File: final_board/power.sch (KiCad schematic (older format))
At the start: 3 parts, among them U501 MCP1755-33, U502 MCP1755-5

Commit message: Changed CAN Chip, added capacitors, added reference
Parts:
- added C501, C503: 10μ, Capacitors_SMD:C_0805_HandSoldering, symbol C
- added C502, C504: .1μ, Capacitors_SMD:C_0603_HandSoldering, symbol C
- gave numbers to parts that had none: 1
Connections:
- wire segments 12 -> 20
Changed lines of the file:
@@
 EESchema Schematic File Version 2
-LIBS:final_outline-rescue
 LIBS:power
 LIBS:device
@@
 $EndComp
 $Comp
-L GND #PWR019
+L GND #PWR017
 U 1 1 563E6C39
 P 5350 3700
-F 0 "#PWR019" H 5350 3450 50  0001 C CNN
+F 0 "#PWR017" H 5350 3450 50  0001 C CNN
 F 1 "GND" H 5350 3550 50  0000 C CNN
 F 2 "" H 5350 3700 60  0000 C CNN
@@
 $EndComp
 $Comp
-L GND #PWR020
+L GND #PWR018
 U 1 1 5650E5B7
 P 2350 3700
-F 0 "#PWR020" H 2350 3450 50  0001 C CNN
+F 0 "#PWR018" H 2350 3450 50  0001 C CNN
 F 1 "GND" H 2350 3550 50  0000 C CNN
 F 2 "" H 2350 3700 60  0000 C CNN
@@
 +12V
 Wire Wire Line
-	1300 2900 1850 2900
+	1000 2900 1850 2900
 Wire Wire Line
 	1600 2900 1600 3100
@@
 Connection ~ 3550 2900
 $Comp
-L LM7810CT U?
+L LM7810CT U503
 U 1 1 56914C23
 P 2300 1600
-F 0 "U?" H 2100 1800 50  0000 C CNN
+F 0 "U503" H 2100 1800 50  0000 C CNN
 F 1 "LM7810CT" H 2300 1800 50  0000 L CNN
 F 2 "TO-220" H 2300 1700 50  0000 C CIN
@@
 +10V
 $Comp
-L GND #PWR021
+L GND #PWR019
 U 1 1 56914D13
 P 2300 1950
-F 0 "#PWR021" H 2300 1700 50  0001 C CNN
+F 0 "#PWR019" H 2300 1700 50  0001 C CNN
 F 1 "GND" H 2300 1800 50  0000 C CNN
 F 2 "" H 2300 1950 50  0000 C CNN
@@
 Wire Wire Line
 	2300 1950 2300 1850
-Text HLabel 1300 2900 0    60   Input ~ 0
+Text HLabel 1000 2900 0    60   Input ~ 0
 +12V
+$Comp
+L C C503
+U 1 1 569165B3
+P 4100 3200
+F 0 "C503" H 4125 3300 50  0000 L CNN
+F 1 "10μ" H 4125 3100 50  0000 L CNN
+F 2 "Capacitors_SMD:C_0805_HandSoldering" H 4138 3050 50  0001 C CNN
+F 3 "" H 4100 3200 50  0000 C CNN
+	1    4100 3200
+	1    0    0    -1
+$EndComp
+$Comp
+L C C504
+U 1 1 5691663C
+P 4400 3200
+F 0 "C504" H 4425 3300 50  0000 L CNN
+F 1 ".1μ" H 4425 3100 50  0000 L CNN
+F 2 "Capacitors_SMD:C_0603_HandSoldering" H 4438 3050 50  0001 C CNN
+F 3 "" H 4400 3200 50  0000 C CNN
+	1    4400 3200
+	1    0    0    -1
+$EndComp
+$Comp
+L C C502
+U 1 1 56916685
+P 1450 3200
+F 0 "C502" H 1475 3300 50  0000 L CNN
+F 1 ".1μ" H 1475 3100 50  0000 L CNN
+F 2 "Capacitors_SMD:C_0603_HandSoldering" H 1488 3050 50  0001 C CNN
+F 3 "" H 1450 3200 50  0000 C CNN
+	1    1450 3200
+	1    0    0    -1
+$EndComp
+$Comp
+L C C501
+U 1 1 569166FC
+P 1200 3200
+F 0 "C501" H 1225 3300 50  0000 L CNN
+F 1 "10μ" H 1225 3100 50  0000 L CNN
+F 2 "Capacitors_SMD:C_0805_HandSoldering" H 1238 3050 50  0001 C CNN
+F 3 "" H 1200 3200 50  0000 C CNN
+	1    1200 3200
+	1    0    0    -1
+$EndComp
+Wire Wire Line
+	1200 3050 1200 2900
+Connection ~ 1200 2900
+Wire Wire Line
+	1450 3050 1450 2900
+Connection ~ 1450 2900
+Wire Wire Line
+	4400 2900 4400 3050
+Connection ~ 4400 2900
+Wire Wire Line
+	4100 2900 4100 3050
+Connection ~ 4100 2900
+$Comp
+L GND #PWR020
+U 1 1 5691687F
+P 4400 3650
+F 0 "#PWR020" H 4400 3400 50  0001 C CNN
+F 1 "GND" H 4400 3500 50  0000 C CNN
+F 2 "" H 4400 3650 50  0000 C CNN
+F 3 "" H 4400 3650 50  0000 C CNN
+	1    4400 3650
+	1    0    0    -1
+$EndComp
+$Comp
+L GND #PWR021
+U 1 1 569168A1
+P 4100 3650
+F 0 "#PWR021" H 4100 3400 50  0001 C CNN
+F 1 "GND" H 4100 3500 50  0000 C CNN
+F 2 "" H 4100 3650 50  0000 C CNN
+F 3 "" H 4100 3650 50  0000 C CNN
+	1    4100 3650
+	1    0    0    -1
+$EndComp
+$Comp
+L GND #PWR022
+U 1 1 569168C3
+P 1450 3600
+F 0 "#PWR022" H 1450 3350 50  0001 C CNN
+F 1 "GND" H 1450 3450 50  0000 C CNN
+F 2 "" H 1450 3600 50  0000 C CNN
+F 3 "" H 1450 3600 50  0000 C CNN
+	1    1450 3600
+	1    0    0    -1
+$EndComp
+$Comp
+L GND #PWR023
+U 1 1 569168E5
+P 1200 3600
+F 0 "#PWR023" H 1200 3350 50  0001 C CNN
+F 1 "GND" H 1200 3450 50  0000 C CNN
+F 2 "" H 1200 3600 50  0000 C CNN
+F 3 "" H 1200 3600 50  0000 C CNN
+	1    1200 3600
+	1    0    0    -1
+$EndComp
+Wire Wire Line
+	4100 3350 4100 3650
+Wire Wire Line
+	4400 3350 4400 3650
+Wire Wire Line
+	1200 3350 1200 3600
+Wire Wire Line
+	1450 3350 1450 3600
 $EndSCHEMATC

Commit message: Final changes to board
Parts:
- removed U503: LM7810CT, TO-220, symbol LM7810CT
- added C505: 10μ, Capacitors_SMD:C_0805_HandSoldering, symbol C
- added C506: .1μ, Capacitors_SMD:C_0603_HandSoldering, symbol C
- added U503: Zsr1000gta, TO_SOT_Packages_SMD:SOT-223, symbol Zsr1000gta
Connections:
- wire segments 20 -> 27
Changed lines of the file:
@@
 LIBS:MITEVT_power
 LIBS:MITEVT_REG
+LIBS:zsr1000gta
 LIBS:final_outline-cache
 EELAYER 25 0
@@
 $EndComp
 $Comp
-L GND #PWR017
+L GND #PWR018
 U 1 1 563E6C39
 P 5350 3700
-F 0 "#PWR017" H 5350 3450 50  0001 C CNN
+F 0 "#PWR018" H 5350 3450 50  0001 C CNN
 F 1 "GND" H 5350 3550 50  0000 C CNN
 F 2 "" H 5350 3700 60  0000 C CNN
@@
 $EndComp
 $Comp
-L GND #PWR018
+L GND #PWR019
 U 1 1 5650E5B7
 P 2350 3700
-F 0 "#PWR018" H 2350 3450 50  0001 C CNN
+F 0 "#PWR019" H 2350 3450 50  0001 C CNN
 F 1 "GND" H 2350 3550 50  0000 C CNN
 F 2 "" H 2350 3700 60  0000 C CNN
@@
 	2350 3500 2350 3700
 NoConn ~ 2900 3100
-Text HLabel 1900 1550 0    60   Input ~ 0
+Text HLabel 1550 1550 0    60   Input ~ 0
 +12V
 Wire Wire Line
@@
 	3550 2600 3550 2900
 Connection ~ 3550 2900
-$Comp
-L LM7810CT U503
-U 1 1 56914C23
-P 2300 1600
-F 0 "U503" H 2100 1800 50  0000 C CNN
-F 1 "LM7810CT" H 2300 1800 50  0000 L CNN
-F 2 "TO-220" H 2300 1700 50  0000 C CIN
-F 3 "" H 2300 1600 50  0000 C CNN
-	1    2300 1600
-	1    0    0    -1
-$EndComp
-Text HLabel 2700 1550 2    60   Output ~ 0
+Text HLabel 3100 1550 2    60   Output ~ 0
 +10V
 $Comp
-L GND #PWR019
+L GND #PWR020
 U 1 1 56914D13
-P 2300 1950
-F 0 "#PWR019" H 2300 1700 50  0001 C CNN
-F 1 "GND" H 2300 1800 50  0000 C CNN
-F 2 "" H 2300 1950 50  0000 C CNN
-F 3 "" H 2300 1950 50  0000 C CNN
-	1    2300 1950
-	1    0    0    -1
-$EndComp
-Wire Wire Line
-	2300 1950 2300 1850
+P 2250 1950
+F 0 "#PWR020" H 2250 1700 50  0001 C CNN
+F 1 "GND" H 2250 1800 50  0000 C CNN
+F 2 "" H 2250 1950 50  0000 C CNN
+F 3 "" H 2250 1950 50  0000 C CNN
+	1    2250 1950
+	1    0    0    -1
+$EndComp
 Text HLabel 1000 2900 0    60   Input ~ 0
 +12V
@@
 Connection ~ 4100 2900
 $Comp
-L GND #PWR020
+L GND #PWR021
 U 1 1 5691687F
 P 4400 3650
-F 0 "#PWR020" H 4400 3400 50  0001 C CNN
+F 0 "#PWR021" H 4400 3400 50  0001 C CNN
 F 1 "GND" H 4400 3500 50  0000 C CNN
 F 2 "" H 4400 3650 50  0000 C CNN
@@
 $EndComp
 $Comp
-L GND #PWR021
+L GND #PWR022
 U 1 1 569168A1
 P 4100 3650
-F 0 "#PWR021" H 4100 3400 50  0001 C CNN
+F 0 "#PWR022" H 4100 3400 50  0001 C CNN
 F 1 "GND" H 4100 3500 50  0000 C CNN
 F 2 "" H 4100 3650 50  0000 C CNN
@@
 $EndComp
 $Comp
-L GND #PWR022
+L GND #PWR023
 U 1 1 569168C3
 P 1450 3600
-F 0 "#PWR022" H 1450 3350 50  0001 C CNN
+F 0 "#PWR023" H 1450 3350 50  0001 C CNN
 F 1 "GND" H 1450 3450 50  0000 C CNN
 F 2 "" H 1450 3600 50  0000 C CNN
@@
 $EndComp
 $Comp
-L GND #PWR023
+L GND #PWR024
 U 1 1 569168E5
 P 1200 3600
-F 0 "#PWR023" H 1200 3350 50  0001 C CNN
+F 0 "#PWR024" H 1200 3350 50  0001 C CNN
 F 1 "GND" H 1200 3450 50  0000 C CNN
 F 2 "" H 1200 3600 50  0000 C CNN
@@
 Wire Wire Line
 	1450 3350 1450 3600
+Wire Wire Line
+	1900 1550 1550 1550
+Wire Wire Line
+	2700 1550 3100 1550
+$Comp
+L GND #PWR025
+U 1 1 56922780
+P 2400 1950
+F 0 "#PWR025" H 2400 1700 50  0001 C CNN
+F 1 "GND" H 2400 1800 50  0000 C CNN
+F 2 "" H 2400 1950 50  0000 C CNN
+F 3 "" H 2400 1950 50  0000 C CNN
+	1    2400 1950
+	1    0    0    -1
+$EndComp
+Wire Wire Line
+	2250 1850 2250 1950
+Wire Wire Line
+	2400 1850 2400 1950
+$Comp
+L Zsr1000gta U503
+U 1 1 56922D9F
+P 2300 1600
+F 0 "U503" H 2500 1400 50  0000 C CNN
+F 1 "Zsr1000gta" H 2300 1800 50  0000 C CNN
+F 2 "TO_SOT_Packages_SMD:SOT-223" H 2300 1600 50  0001 C CNN
+F 3 "" H 2300 1600 50  0000 C CNN
+	1    2300 1600
+	1    0    0    -1
+$EndComp
+$Comp
+L C C506
+U 1 1 56923C74
+P 3000 1850
+F 0 "C506" H 3025 1950 50  0000 L CNN
+F 1 ".1μ" H 3025 1750 50  0000 L CNN
+F 2 "Capacitors_SMD:C_0603_HandSoldering" H 3038 1700 50  0001 C CNN
+F 3 "" H 3000 1850 50  0000 C CNN
+	1    3000 1850
+	1    0    0    -1
+$EndComp
+$Comp
+L C C505
+U 1 1 56923C7A
+P 2750 1850
+F 0 "C505" H 2775 1950 50  0000 L CNN
+F 1 "10μ" H 2775 1750 50  0000 L CNN
+F 2 "Capacitors_SMD:C_0805_HandSoldering" H 2788 1700 50  0001 C CNN
+F 3 "" H 2750 1850 50  0000 C CNN
+	1    2750 1850
+	1    0    0    -1
+$EndComp
+$Comp
+L GND #PWR?
+U 1 1 56923C80
+P 3000 2250
+F 0 "#PWR?" H 3000 2000 50  0001 C CNN
+F 1 "GND" H 3000 2100 50  0000 C CNN
+F 2 "" H 3000 2250 50  0000 C CNN
+F 3 "" H 3000 2250 50  0000 C CNN
+	1    3000 2250
+	1    0    0    -1
+$EndComp
+$Comp
+L GND #PWR?
+U 1 1 56923C86
+P 2750 2250
+F 0 "#PWR?" H 2750 2000 50  0001 C CNN
+F 1 "GND" H 2750 2100 50  0000 C CNN
+F 2 "" H 2750 2250 50  0000 C CNN
+F 3 "" H 2750 2250 50  0000 C CNN
+	1    2750 2250
+	1    0    0    -1
+$EndComp
+Wire Wire Line
+	2750 2000 2750 2250
+Wire Wire Line
+	3000 2000 3000 2250
+Wire Wire Line
+	2750 1700 2750 1550
+Connection ~ 2750 1550
+Wire Wire Line
+	3000 1700 3000 1550
+Connection ~ 3000 1550
 $EndSCHEMATC

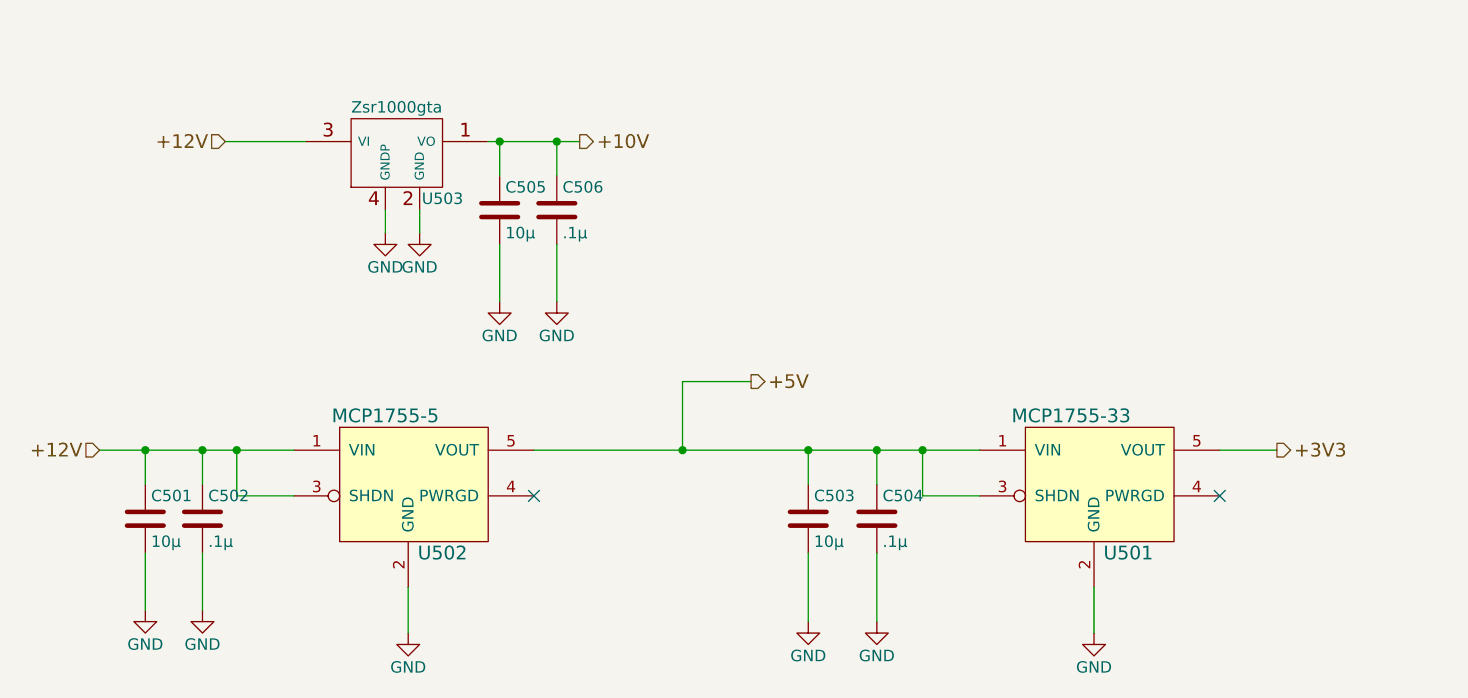
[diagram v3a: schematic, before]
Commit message: Updated PCB by replacing old parts, fixing voltage regulator, adding test points, and general improvements
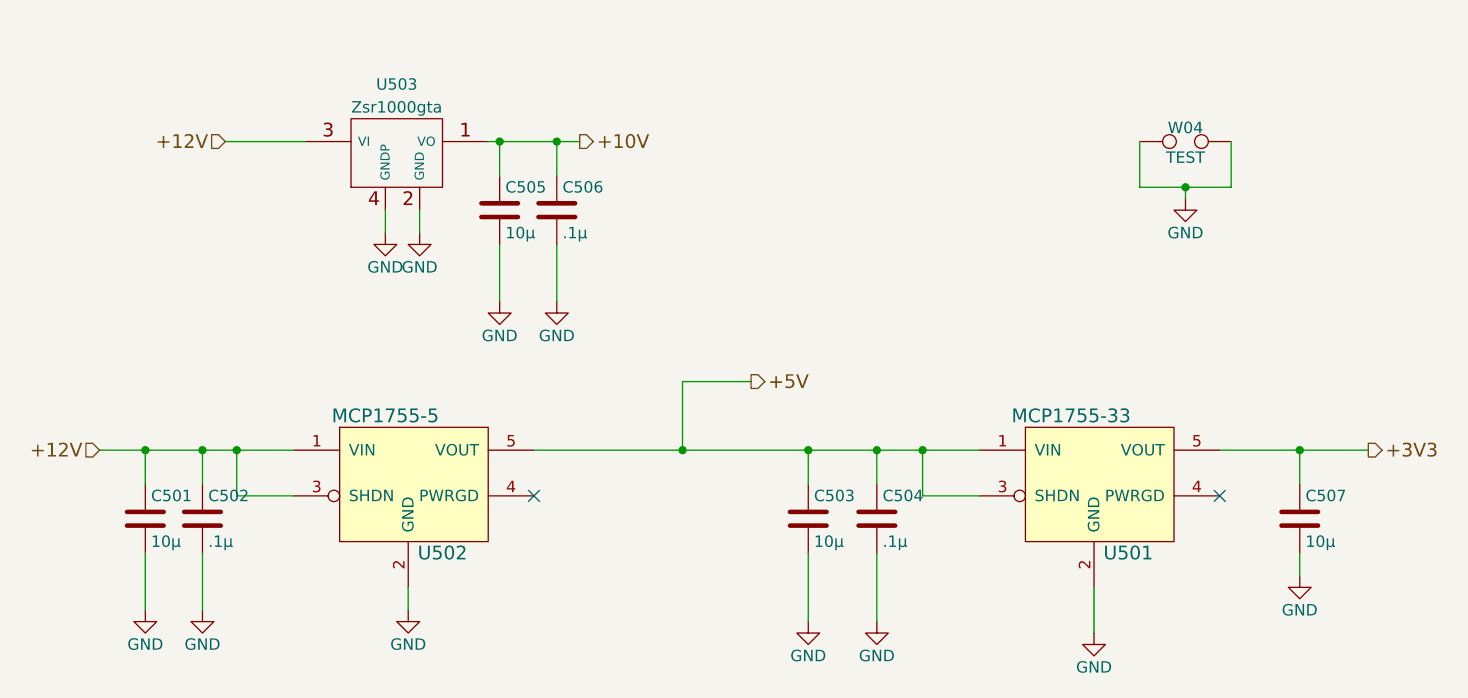
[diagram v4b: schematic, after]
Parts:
- added C507: 10μ, Capacitors_SMD:C_0805_HandSoldering, symbol C
- added W04: TEST, Measurement_Points:Test_Point_2Pads, symbol TEST
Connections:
- net +3V3: now also C507.1
- net GND: now also C507.2, W04.1, W04.2
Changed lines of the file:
@@
 $EndComp
 $Comp
-L GND #PWR018
+L GND #PWR026
 U 1 1 563E6C39
 P 5350 3700
-F 0 "#PWR018" H 5350 3450 50  0001 C CNN
+F 0 "#PWR026" H 5350 3450 50  0001 C CNN
 F 1 "GND" H 5350 3550 50  0000 C CNN
 F 2 "" H 5350 3700 60  0000 C CNN
@@
 	4600 3100 4850 3100
 Connection ~ 4600 2900
-Text HLabel 6150 2900 2    60   Output ~ 0
+Text HLabel 6550 2900 2    60   Output ~ 0
 +3V3
 Wire Wire Line
-	6150 2900 5900 2900
+	5900 2900 6550 2900
 $Comp
 L MCP1755 U502
@@
 $EndComp
 $Comp
-L GND #PWR019
+L GND #PWR027
 U 1 1 5650E5B7
-P 2350 3700
-F 0 "#PWR019" H 2350 3450 50  0001 C CNN
-F 1 "GND" H 2350 3550 50  0000 C CNN
-F 2 "" H 2350 3700 60  0000 C CNN
-F 3 "" H 2350 3700 60  0000 C CNN
-	1    2350 3700
-	1    0    0    -1
-$EndComp
-Wire Wire Line
-	2350 3500 2350 3700
+P 2350 3600
+F 0 "#PWR027" H 2350 3350 50  0001 C CNN
+F 1 "GND" H 2350 3450 50  0000 C CNN
+F 2 "" H 2350 3600 60  0000 C CNN
+F 3 "" H 2350 3600 60  0000 C CNN
+	1    2350 3600
+	1    0    0    -1
+$EndComp
 NoConn ~ 2900 3100
 Text HLabel 1550 1550 0    60   Input ~ 0
@@
 +10V
 $Comp
-L GND #PWR020
+L GND #PWR028
 U 1 1 56914D13
 P 2250 1950
-F 0 "#PWR020" H 2250 1700 50  0001 C CNN
+F 0 "#PWR028" H 2250 1700 50  0001 C CNN
 F 1 "GND" H 2250 1800 50  0000 C CNN
 F 2 "" H 2250 1950 50  0000 C CNN
@@
 Connection ~ 4100 2900
 $Comp
-L GND #PWR021
+L GND #PWR029
 U 1 1 5691687F
 P 4400 3650
-F 0 "#PWR021" H 4400 3400 50  0001 C CNN
+F 0 "#PWR029" H 4400 3400 50  0001 C CNN
 F 1 "GND" H 4400 3500 50  0000 C CNN
 F 2 "" H 4400 3650 50  0000 C CNN
@@
 $EndComp
 $Comp
-L GND #PWR022
+L GND #PWR030
 U 1 1 569168A1
 P 4100 3650
-F 0 "#PWR022" H 4100 3400 50  0001 C CNN
+F 0 "#PWR030" H 4100 3400 50  0001 C CNN
 F 1 "GND" H 4100 3500 50  0000 C CNN
 F 2 "" H 4100 3650 50  0000 C CNN
@@
 $EndComp
 $Comp
-L GND #PWR023
+L GND #PWR031
 U 1 1 569168C3
 P 1450 3600
-F 0 "#PWR023" H 1450 3350 50  0001 C CNN
+F 0 "#PWR031" H 1450 3350 50  0001 C CNN
 F 1 "GND" H 1450 3450 50  0000 C CNN
 F 2 "" H 1450 3600 50  0000 C CNN
@@
 $EndComp
 $Comp
-L GND #PWR024
+L GND #PWR032
 U 1 1 569168E5
 P 1200 3600
-F 0 "#PWR024" H 1200 3350 50  0001 C CNN
+F 0 "#PWR032" H 1200 3350 50  0001 C CNN
 F 1 "GND" H 1200 3450 50  0000 C CNN
 F 2 "" H 1200 3600 50  0000 C CNN
@@
 	2700 1550 3100 1550
 $Comp
-L GND #PWR025
+L GND #PWR033
 U 1 1 56922780
 P 2400 1950
-F 0 "#PWR025" H 2400 1700 50  0001 C CNN
+F 0 "#PWR033" H 2400 1700 50  0001 C CNN
 F 1 "GND" H 2400 1800 50  0000 C CNN
 F 2 "" H 2400 1950 50  0000 C CNN
@@
 U 1 1 56922D9F
 P 2300 1600
-F 0 "U503" H 2500 1400 50  0000 C CNN
+F 0 "U503" H 2300 1900 50  0000 C CNN
 F 1 "Zsr1000gta" H 2300 1800 50  0000 C CNN
 F 2 "TO_SOT_Packages_SMD:SOT-223" H 2300 1600 50  0001 C CNN
@@
 $EndComp
 $Comp
-L GND #PWR026
+L GND #PWR034
 U 1 1 56923C80
 P 3000 2250
-F 0 "#PWR026" H 3000 2000 50  0001 C CNN
+F 0 "#PWR034" H 3000 2000 50  0001 C CNN
 F 1 "GND" H 3000 2100 50  0000 C CNN
 F 2 "" H 3000 2250 50  0000 C CNN
@@
 $EndComp
 $Comp
-L GND #PWR027
+L GND #PWR035
 U 1 1 56923C86
 P 2750 2250
-F 0 "#PWR027" H 2750 2000 50  0001 C CNN
+F 0 "#PWR035" H 2750 2000 50  0001 C CNN
 F 1 "GND" H 2750 2100 50  0000 C CNN
 F 2 "" H 2750 2250 50  0000 C CNN
@@
 	3000 1700 3000 1550
 Connection ~ 3000 1550
+$Comp
+L C C507
+U 1 1 5825A458
+P 6250 3200
+F 0 "C507" H 6275 3300 50  0000 L CNN
+F 1 "10μ" H 6275 3100 50  0000 L CNN
+F 2 "Capacitors_SMD:C_0805_HandSoldering" H 6288 3050 50  0001 C CNN
+F 3 "" H 6250 3200 50  0000 C CNN
+	1    6250 3200
+	1    0    0    -1
+$EndComp
+Wire Wire Line
+	6250 3050 6250 2900
+Connection ~ 6250 2900
+Wire Wire Line
+	6250 3350 6250 3450
+$Comp
+L GND #PWR036
+U 1 1 5825A5A4
+P 6250 3450
+F 0 "#PWR036" H 6250 3200 50  0001 C CNN
+F 1 "GND" H 6250 3300 50  0000 C CNN
+F 2 "" H 6250 3450 50  0000 C CNN
+F 3 "" H 6250 3450 50  0000 C CNN
+	1    6250 3450
+	1    0    0    -1
+$EndComp
+Wire Wire Line
+	2350 3500 2350 3600
+$Comp
+L TEST W04
+U 1 1 5827D5C6
+P 5750 1550
+F 0 "W04" H 5750 1610 50  0000 C CNN
+F 1 "TEST" H 5750 1480 50  0000 C CNN
+F 2 "Measurement_Points:Test_Point_2Pads" H 5750 1550 50  0001 C CNN
+F 3 "" H 5750 1550 50  0000 C CNN
+	1    5750 1550
+	1    0    0    -1
+$EndComp
+Wire Wire Line
+	5550 1550 5550 1750
+Wire Wire Line
+	5550 1750 5950 1750
+Wire Wire Line
+	5950 1750 5950 1550
+Wire Wire Line
+	5750 1750 5750 1800
+Connection ~ 5750 1750
+$Comp
+L GND #PWR037
+U 1 1 5827D7E1
+P 5750 1800
+F 0 "#PWR037" H 5750 1550 50  0001 C CNN
+F 1 "GND" H 5750 1650 50  0000 C CNN
+F 2 "" H 5750 1800 50  0000 C CNN
+F 3 "" H 5750 1800 50  0000 C CNN
+	1    5750 1800
+	1    0    0    -1
+$EndComp
 $EndSCHEMATC
